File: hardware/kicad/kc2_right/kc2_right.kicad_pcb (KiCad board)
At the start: 2 copper layers, 194 x 133.8 mm, 94 parts, among them SW1 KEY_01, SW10 KEY_10, SW11 KEY_11, SW12 KEY_12, SW13 KEY_13, SW14 KEY_14, SW15 KEY_15, SW16 KEY_16, SW17 KEY_17, SW18 KEY_18, SW19 KEY_19, SW2 KEY_02, SW20 KEY_20, SW21 KEY_21, SW22 KEY_22, SW23 KEY_23, SW24 KEY_24, SW25 KEY_25, SW26 KEY_26, SW27 KEY_27, SW28 KEY_28, SW29 KEY_29, SW3 KEY_03, SW30 KEY_30, SW31 KEY_31, SW32 KEY_32, SW33 KEY_33, SW34 KEY_34, SW35 KEY_35, SW36 KEY_36, SW37 KEY_37, SW38 KEY_38, SW39 KEY_39, SW4 KEY_04, SW40 KEY_40, SW41 KEY_41, SW5 KEY_05, SW6 KEY_06, SW7 KEY_07, SW8 KEY_08, SW9 KEY_09, U1 nice!nano_v2_socket_24pin

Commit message: Finalize KC2 routed PCB draft
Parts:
- moved H3 6.00 mm to (70.0, 44.0)
- moved H4 6.00 mm to (106.0, 44.0)
- moved J_PWR1 6.00 mm to (116.0, 50.0)
- moved SW_RST1 6.00 mm to (97.9, 62.1)
- moved U1 6.00 mm to (88.0, 49.0)
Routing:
- net R_COL4: track 211.2 -> 170.8 mm
- net R_ROW1: track 245.0 -> 205.6 mm, vias 8 -> 1
- net R_ROW4: track 282.3 -> 250.8 mm, vias 8 -> 2
- net R_ROW2: track 252.4 -> 222.5 mm, vias 8 -> 1
- net R_ROW0: track 202.4 -> 177.1 mm, vias 5 -> 0
- net R_ROW3: track 253.7 -> 230.5 mm, vias 8 -> 1
- net R_COL6: track 255.5 -> 234.0 mm, vias 1 -> 2
- net R_COL5: track 223.5 -> 202.0 mm, vias 2 -> 1
- net R_COL3: track 183.8 -> 168.1 mm
- net RST: track 35.9 -> 23.2 mm, vias 1 -> 0
- net R_COL7: track 275.0 -> 262.6 mm
- net R_COL1: track 146.3 -> 136.2 mm
- net R_COL8: track 179.8 -> 187.9 mm, vias 2 -> 1
- net R_COL2: track 172.2 -> 166.1 mm, vias 2 -> 1
- net RK17_D: track 14.9 -> 12.0 mm, vias 1 -> 0
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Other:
- outline, holes or cut-outs redrawn

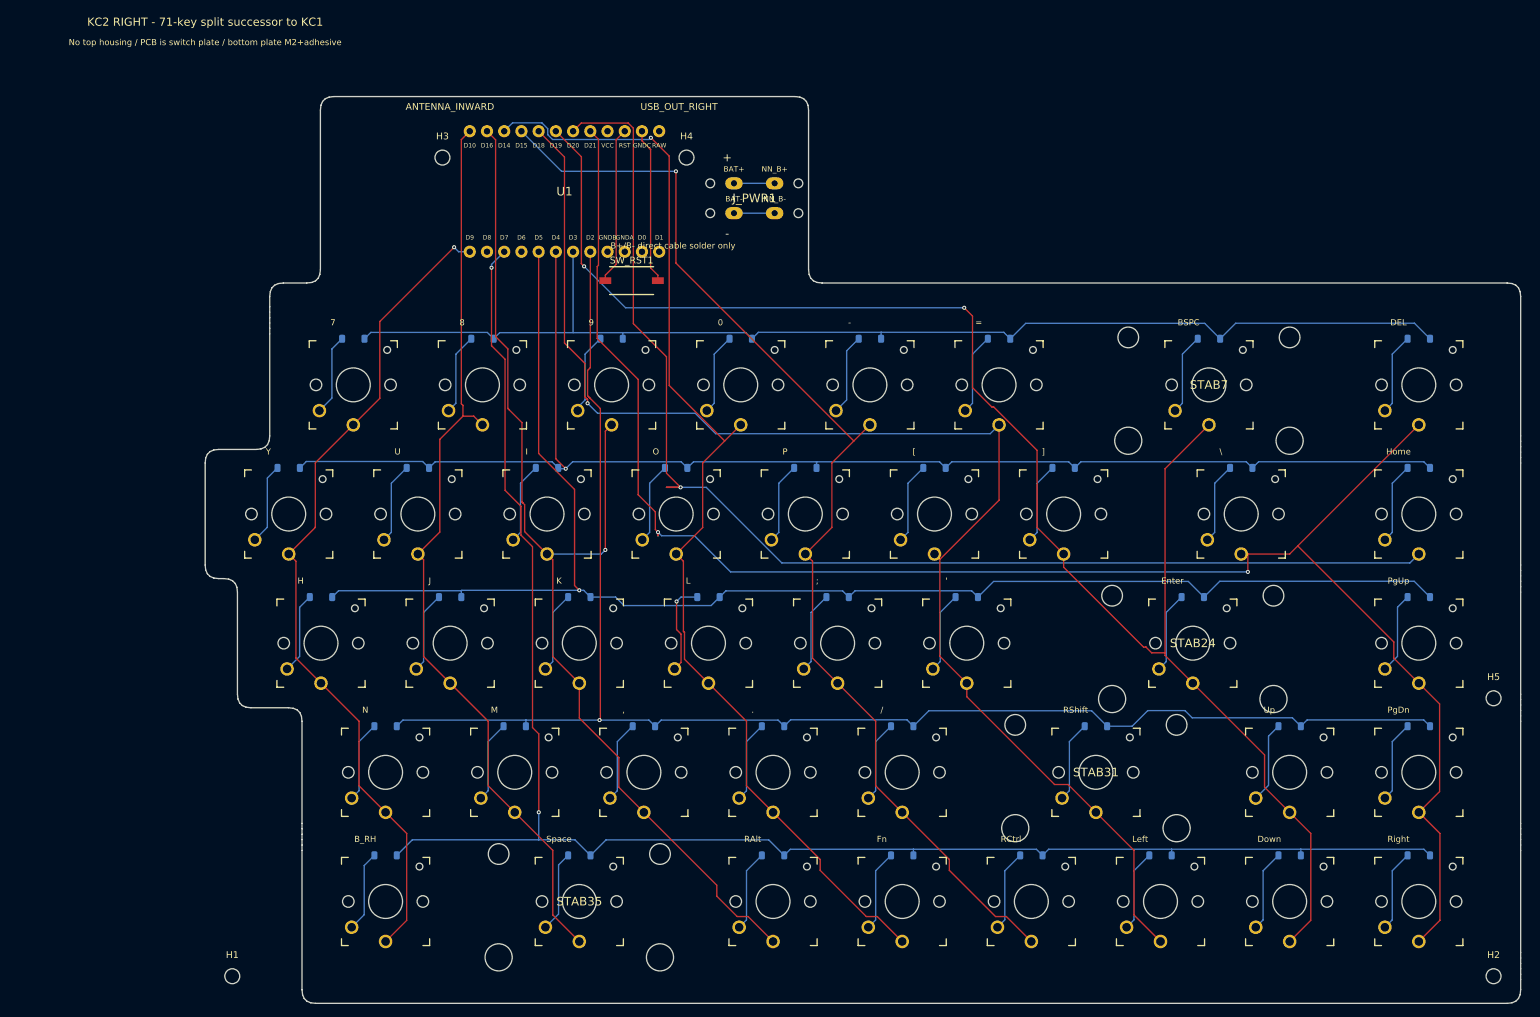
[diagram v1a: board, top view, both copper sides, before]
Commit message: chore: OPS-ARCH-002 KC2 X3 KiCad 산출물을 main 경로로 승격한다
- X3 좌우 프로젝트를 hardware/kicad/kc2_left, hardware/kicad/kc2_right로 승격
- soldered, hotswap, x1, x2 변형은 hardware/kicad/draft 아래에 보존
- manifest, autoroute, file naming, fabrication ZIP, renders, verify scripts를 main 경로 기준으로 갱신
- SRS evidence와 OPS-ARCH-002 verified 상태를 반영
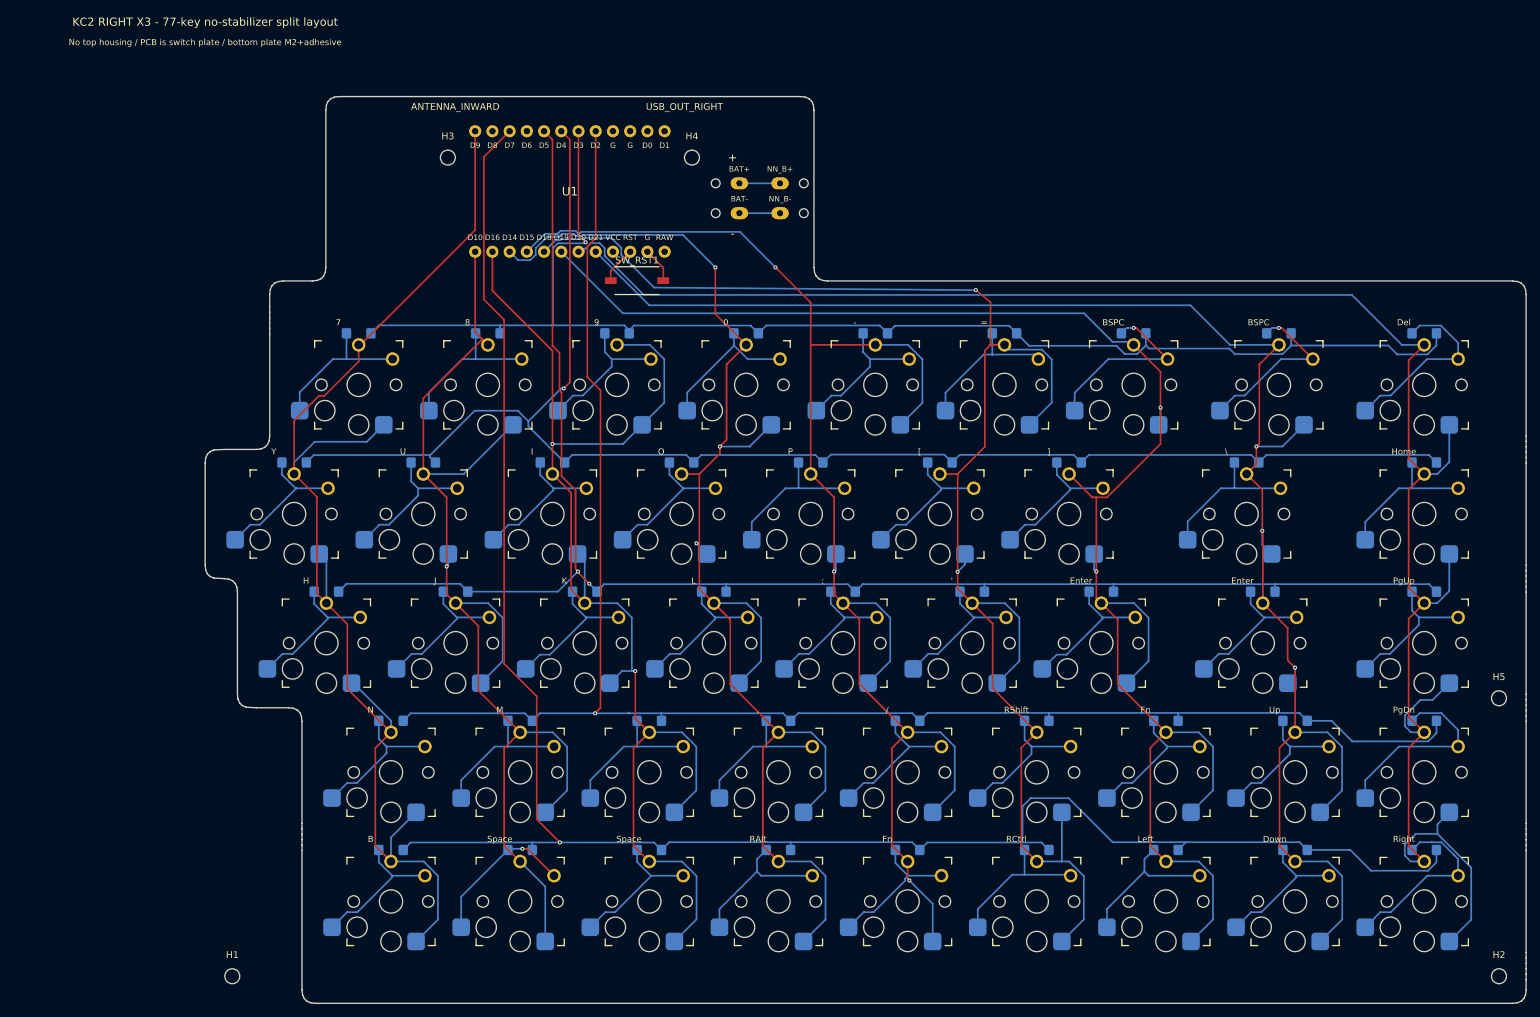
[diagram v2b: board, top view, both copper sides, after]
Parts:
- removed STAB24: PCB_mount_stab_for_2.50u, KC2:PCB_Mount_2u_Stabilizer_NPTH
- removed STAB31, STAB35: PCB_mount_stab_for_2.00u, KC2:PCB_Mount_2u_Stabilizer_NPTH
- removed STAB7: PCB_mount_stab_for_2.25u, KC2:PCB_Mount_2u_Stabilizer_NPTH
- added D42: 1N4148W_SOD123_DeviceMart_14592018, D_SOD123_HandSolder_14592018, B.Cu at (157.7, 146.1)
- added D43: 1N4148W_SOD123_DeviceMart_14592018, D_SOD123_HandSolder_14592018, B.Cu at (176.7, 146.1)
- added D44: 1N4148W_SOD123_DeviceMart_14592018, D_SOD123_HandSolder_14592018, B.Cu at (195.8, 146.1)
- added D45: 1N4148W_SOD123_DeviceMart_14592018, D_SOD123_HandSolder_14592018, B.Cu at (214.8, 146.1)
- added SW42: KEY_42, SW_Kailh_Choc_V1_HotSwap_THT, F.Cu at (157.7, 153.7)
- added SW43: KEY_43, SW_Kailh_Choc_V1_HotSwap_THT, F.Cu at (176.7, 153.7)
- added SW44: KEY_44, SW_Kailh_Choc_V1_HotSwap_THT, F.Cu at (195.8, 153.7)
- added SW45: KEY_45, SW_Kailh_Choc_V1_HotSwap_THT, F.Cu at (214.8, 153.7)
- D1, D10, D11, D12, D13, D14, D15, D16, D17, D18, D19, D2, D20, D21, D22, D23, D24, D25, D26, D27, D28, D29, D3, D30, D31, D32, D33, D34, D35, D36, D37, D38, D39, D4, D40, D41, D5, D6, D7, D8, D9: value 1N4148W_SOD-123 -> 1N4148W_SOD123_DeviceMart_14592018; footprint D_SOD-123 -> D_SOD123_HandSolder_14592018
- SW1, SW10, SW11, SW12, SW13, SW14, SW15, SW16, SW17, SW18, SW19, SW2, SW20, SW21, SW22, SW23, SW24, SW25, SW26, SW27, SW28, SW29, SW3, SW30, SW31, SW32, SW33, SW34, SW35, SW36, SW37, SW38, SW39, SW4, SW40, SW41, SW5, SW6, SW7, SW8, SW9: footprint SW_Kailh_Choc_V1V2_THT_Hybrid -> SW_Kailh_Choc_V1_HotSwap_THT
- U1: footprint KC2:NiceNanoV2_Socket_24Pin -> KC2:NiceNanoV2_Socket_24Pin_USB_OUT_RIGHT
- moved D9 168.7 mm to (214.8, 69.9)
- moved SW9 168.6 mm to (214.8, 77.5)
- moved D18 163.9 mm to (214.8, 89.0)
- moved SW18 163.8 mm to (214.8, 96.6)
- moved D27 135.6 mm to (214.8, 108.0)
- moved SW27 135.5 mm to (214.8, 115.6)
- moved D26 130.9 mm to (191.0, 108.0)
- moved SW26 130.8 mm to (191.0, 115.6)
- moved D34 116.8 mm to (176.7, 127.1)
- moved SW34 116.7 mm to (176.7, 134.7)
- moved D35 107.4 mm to (195.8, 127.1)
- moved SW35 107.3 mm to (195.8, 134.7)
- moved D36 98.1 mm to (214.8, 127.1)
- moved SW36 97.9 mm to (214.8, 134.7)
- moved D37 75.4 mm to (62.4, 146.1)
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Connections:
- D18 pad 1: R_ROW2 -> R_ROW1
- D26 pad 1: R_ROW3 -> R_ROW2
- D27 pad 1: R_ROW3 -> R_ROW2
- D34 pad 1: R_ROW4 -> R_ROW3
- D35 pad 1: R_ROW4 -> R_ROW3
- D36 pad 1: R_ROW4 -> R_ROW3
- D9 pad 1: R_ROW1 -> R_ROW0
- SW10 pad 1: R_COL1 -> R_COL0
- SW11 pad 1: R_COL2 -> R_COL1
- SW12 pad 1: R_COL3 -> R_COL2
- SW13 pad 1: R_COL4 -> R_COL3
- SW14 pad 1: R_COL5 -> R_COL4
- SW15 pad 1: R_COL6 -> R_COL5
- SW16 pad 1: R_COL7 -> R_COL6
- SW17 pad 1: R_COL8 -> R_COL7
- SW18 pad 1: R_COL0 -> R_COL8
- SW19 pad 1: R_COL1 -> R_COL0
- SW20 pad 1: R_COL2 -> R_COL1
- SW21 pad 1: R_COL3 -> R_COL2
- SW22 pad 1: R_COL4 -> R_COL3
- SW23 pad 1: R_COL5 -> R_COL4
- SW24 pad 1: R_COL6 -> R_COL5
- SW25 pad 1: R_COL7 -> R_COL6
- SW26 pad 1: R_COL0 -> R_COL7
- SW27 pad 1: R_COL1 -> R_COL8
- SW28 pad 1: R_COL2 -> R_COL0
- SW29 pad 1: R_COL3 -> R_COL1
- SW30 pad 1: R_COL4 -> R_COL2
- SW31 pad 1: R_COL5 -> R_COL3
- SW32 pad 1: R_COL6 -> R_COL4
- SW33 pad 1: R_COL7 -> R_COL5
- SW34 pad 1: R_COL0 -> R_COL6
- SW35 pad 1: R_COL1 -> R_COL7
- SW36 pad 1: R_COL2 -> R_COL8
- SW37 pad 1: R_COL3 -> R_COL0
- SW38 pad 1: R_COL4 -> R_COL1
- SW39 pad 1: R_COL5 -> R_COL2
- SW40 pad 1: R_COL6 -> R_COL3
- SW41 pad 1: R_COL7 -> R_COL4
- SW9 pad 1: R_COL0 -> R_COL8
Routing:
- net R_COL8: track 187.9 -> 282.5 mm, vias 1 -> 0
- net R_COL0: track 123.6 -> 189.6 mm, vias 1 -> 0
- net R_COL4: track 170.8 -> 220.3 mm, vias 1 -> 3
- net R_COL3: track 168.1 -> 205.2 mm, vias 1 -> 3
- net R_COL1: track 136.2 -> 172.2 mm, vias 0 -> 1
- net R_ROW4: track 250.8 -> 286.7 mm, vias 2 -> 1
- net R_COL5: track 202.0 -> 233.7 mm, vias 1 -> 2
- net R_ROW0: track 177.1 -> 204.9 mm, vias 0 -> 1
- net RK45_D: track 0.00 -> 27.6 mm
- net RK43_D: track 0.00 -> 22.7 mm
- net RK42_D: track 0.00 -> 22.2 mm
- net RK44_D: track 0.00 -> 21.6 mm
- net R_COL2: track 166.1 -> 187.2 mm, vias 1 -> 2
- net R_ROW1: track 205.6 -> 226.5 mm
- net R_COL7: track 262.6 -> 242.2 mm, vias 2 -> 3
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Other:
- board size 194 x 133.8 mm -> 194.8 x 133.8 mm
- board text added: "B"
- board text added: "Del"
- board text added: "KC2 RIGHT X3 - 77-key no-stabilizer split layout"
- board text added: "X3: X2 electrical stack, no-stabilizer 77-key split layout"
- board text removed: "B_RH"
- board text removed: "DEL"
- board text removed: "KC2 RIGHT - 71-key split successor to KC1"

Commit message: fix: KC2 X3 탭 축소로 nice!nano 안테나 keepout 충돌 해소
배터리 carrier 패드와 불필요한 전원 넷을 제거해 컨트롤러 탭을 축소
reset 스위치 위치와 후처리 라우팅을 조정해 nice!nano 안테나 keepout 및 M2 홀 간섭을 해소
검증기, DRC, 렌더, Gerber, JLCPCB ZIP, docs/spec 증거를 갱신
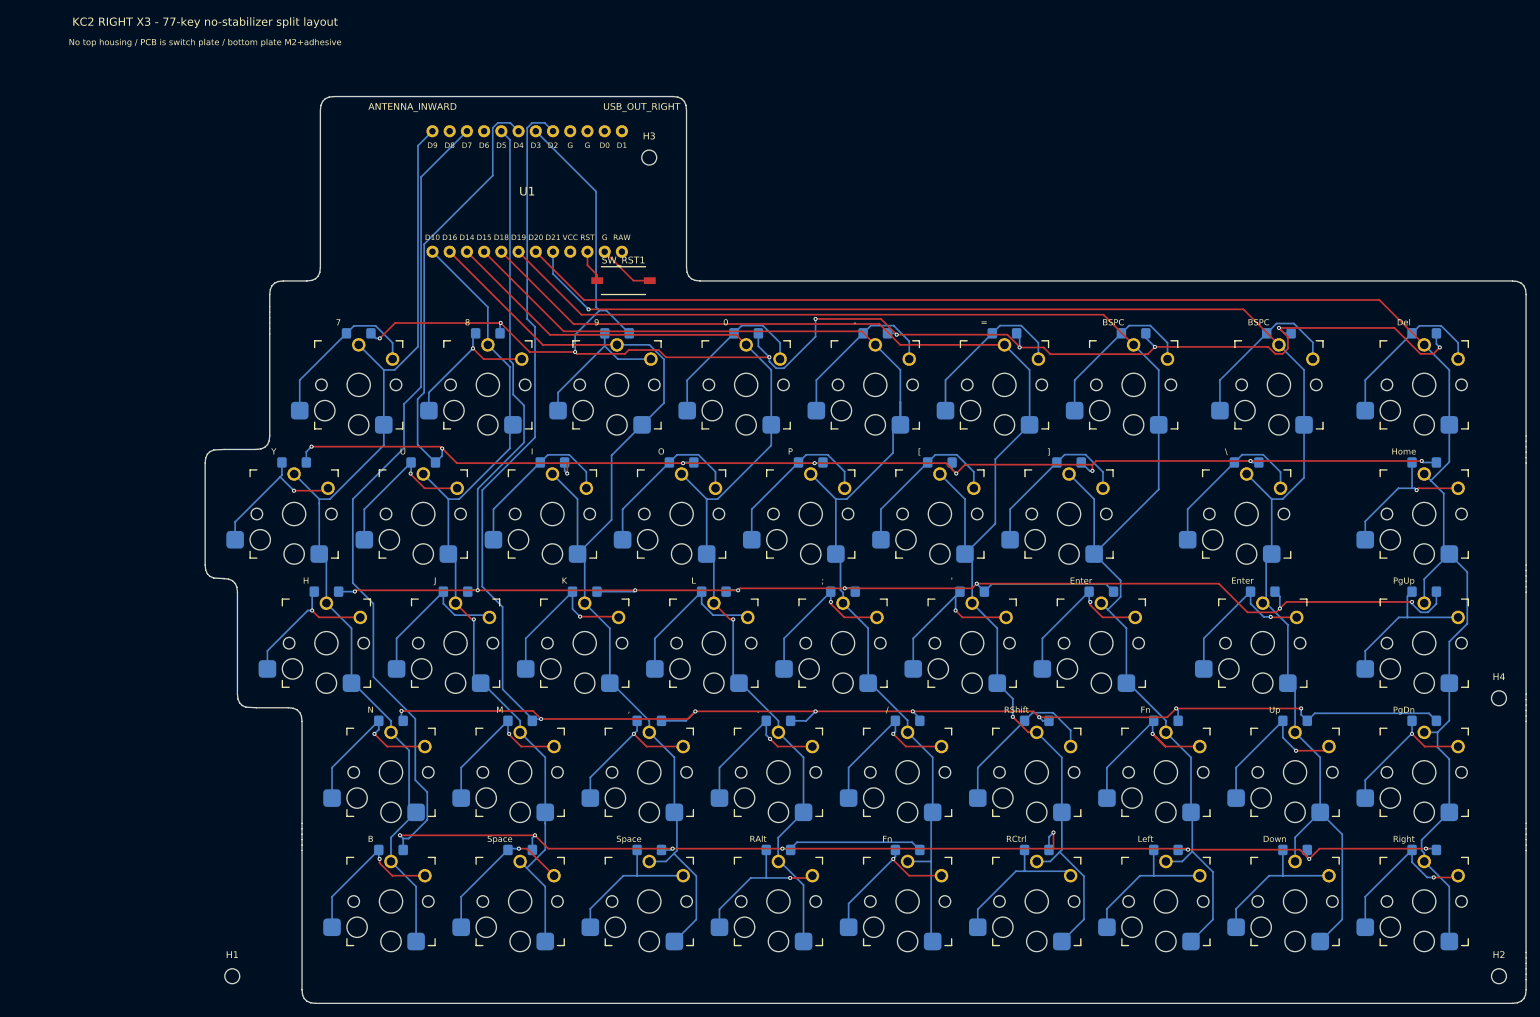
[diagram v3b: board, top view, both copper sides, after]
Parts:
- removed H5: M2_NPTH_2.2, MountingHole_2.2mm_M2
- removed J_PWR1: BAT_NN_direct_solder, KC2:DirectSolderPowerPads
- moved H4 143.3 mm to (225.8, 123.8)
- moved H3 29.7 mm to (100.5, 44.0)
- moved U1 6.30 mm to (82.5, 49.0)
- moved SW_RST1 2.00 mm to (96.7, 62.1)
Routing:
- net R_COL3: track 205.2 -> 156.1 mm, vias 3 -> 1
- net R_COL1: track 172.2 -> 127.0 mm
- net R_COL4: track 220.3 -> 176.1 mm, vias 3 -> 0
- net R_COL0: track 189.6 -> 147.9 mm
- net R_ROW2: track 238.7 -> 275.1 mm, vias 2 -> 8
- net R_COL8: track 282.5 -> 247.8 mm
- net R_COL5: track 233.7 -> 200.3 mm, vias 2 -> 1
- net R_ROW0: track 204.9 -> 237.5 mm, vias 1 -> 10
- net R_COL2: track 187.2 -> 155.9 mm, vias 2 -> 0
- net R_COL6: track 246.3 -> 219.4 mm, vias 2 -> 0
- net R_ROW4: track 286.7 -> 310.1 mm, vias 1 -> 8
- net R_ROW3: track 250.6 -> 273.6 mm, vias 1 -> 8
- net R_ROW1: track 226.5 -> 245.7 mm, vias 1 -> 9
- net R_COL7: track 242.2 -> 228.0 mm, vias 3 -> 1
- net RK34_D: track 21.6 -> 29.3 mm, vias 0 -> 1
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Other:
- outline, holes or cut-outs redrawn
- board text added: "Battery solders directly to nice!nano B+/B-; no carrier power pads"
- board text removed: "+"
- board text removed: "B+/B- direct cable solder only"
